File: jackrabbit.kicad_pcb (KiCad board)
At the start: 2 copper layers, 50.3 x 55.4 mm, 56 parts, among them J1 USB_C, J2 PinHeader_2.54mm_02x08, J3 PinHeader_2.54mm_02x08, J4 PinHeader_2.54mm_02x04, J5 PinHeader_2.54mm_02x04, J6 JST_SH_01x04_SM04B-SRSS-TB, J7 PinHeader_2.54mm_01x03, SW1 SW_Push, SW2 SW_Push, U1 MIC5319-3.3YD5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

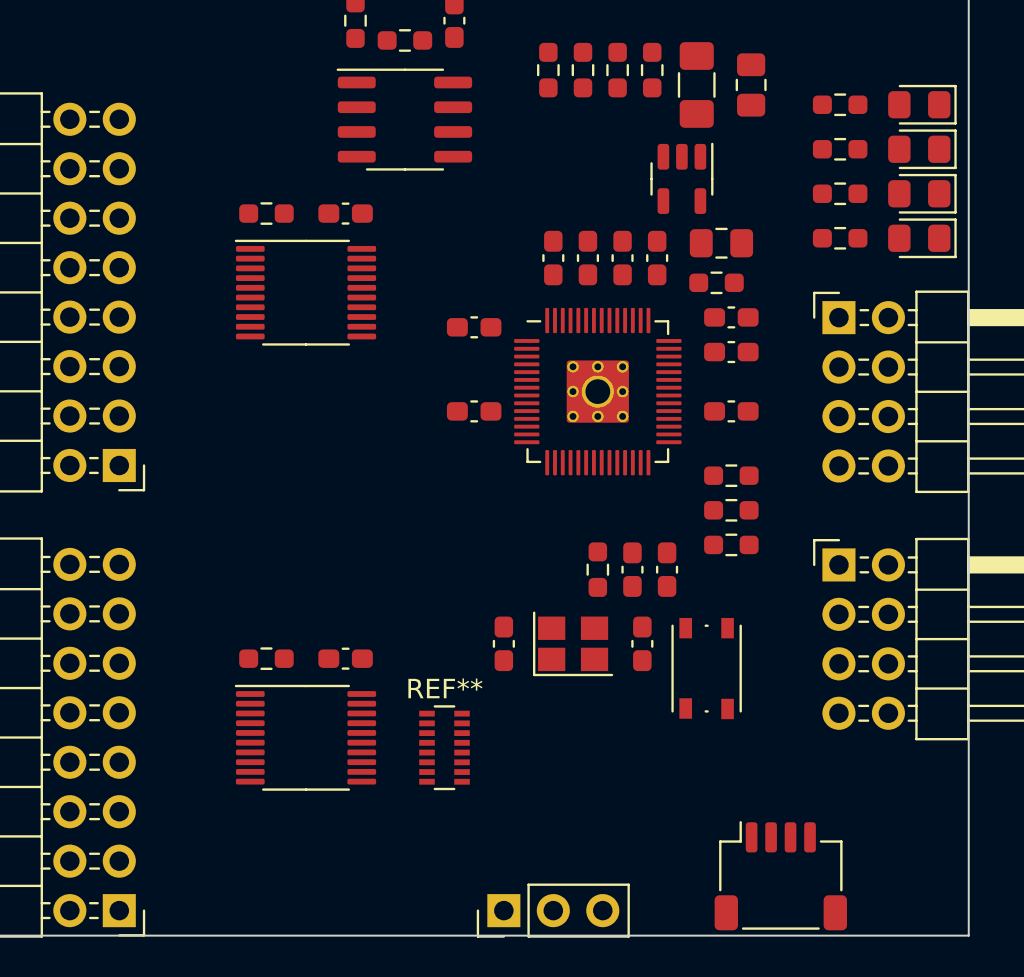
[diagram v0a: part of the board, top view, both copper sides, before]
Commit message: Add bus contention series protection resistors
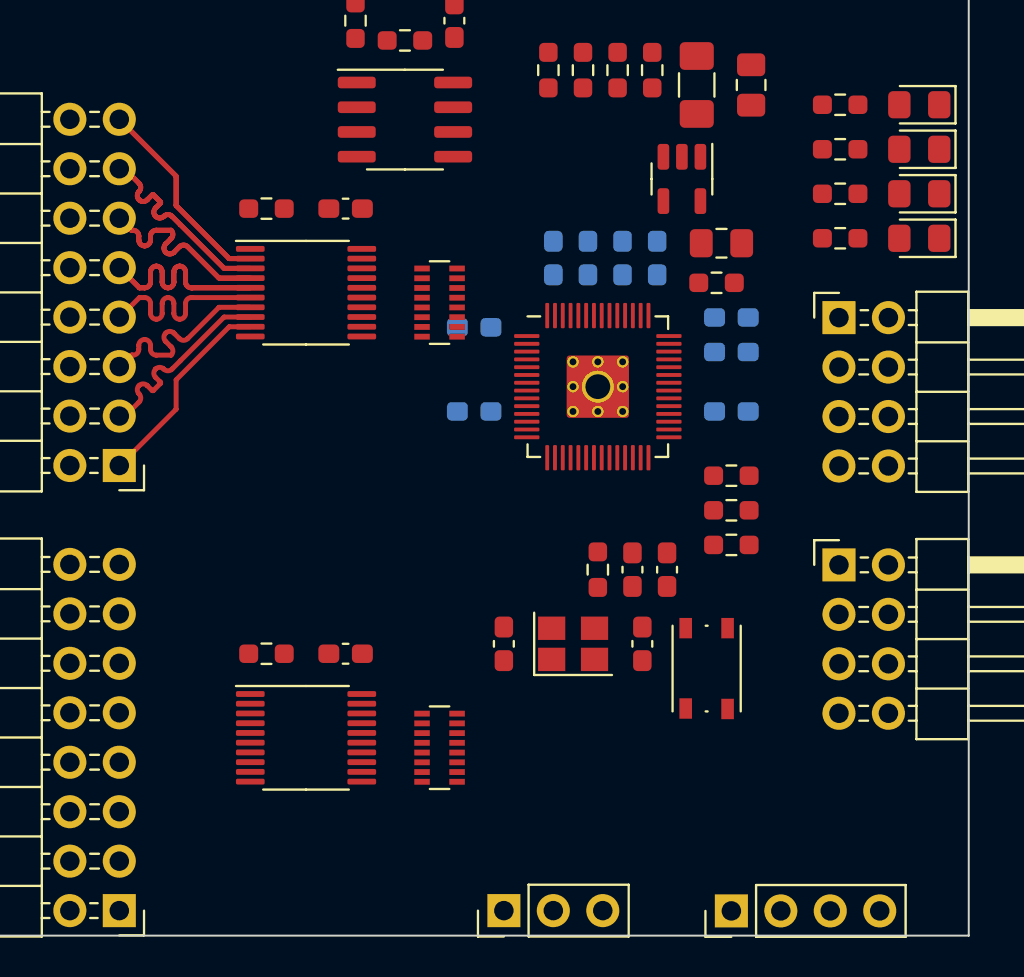
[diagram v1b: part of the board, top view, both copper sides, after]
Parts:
- removed REF**: R_Array_Convex_8x0602, Resistor_SMD:R_Array_Convex_8x0602
- added RN1: 220, Resistor_SMD:R_Array_Convex_8x0602, F.Cu at (144.0, 109.7)
- added RN2: 220, Resistor_SMD:R_Array_Convex_8x0602, F.Cu at (144.0, 132.6)
- C1, C10, C13, C14, C4, C5, C6, C8, C9: moved to B.Cu
- J6: value JST_SH_01x04_SM04B-SRSS-TB -> PinHeader_2.54mm_01x04; footprint Connector_JST:JST_SH_SM04B-SRSS-TB_1x04-1MP_P1.00mm_Horizontal -> Connector_PinHeader_2.54mm:PinHeader_1x04_P2.54mm_Vertical
- R7, R8: value 2.2k -> 100
- moved J6 3.10 mm to (159.0, 141.0), turned to 90 degrees
- moved C11 0.25 mm to (139.2, 104.9)
- moved R9 0.25 mm to (135.1, 104.9)
- moved C16 0.25 mm to (139.2, 127.8)
- moved R12 0.25 mm to (135.1, 127.8)
- moved U4 0.25 mm to (152.1, 114.0)
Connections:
- J6 pad 1: /RX/SDA -> /RX
- J6 pad 2: /TX/SCL -> /TX
- R7 pad 1: /TX/SCL -> Net-(R7-Pad1)
- R7 pad 2: +3V3 -> /TX
- R8 pad 1: /RX/SDA -> Net-(R8-Pad1)
- R8 pad 2: +3V3 -> /RX
- U2 pad 11: /DIG7 -> Net-(RN1-Pad8)
- U2 pad 12: /DIG6 -> Net-(RN1-Pad7)
- U2 pad 13: /DIG5 -> Net-(RN1-Pad6)
- U2 pad 14: /DIG4 -> Net-(RN1-Pad5)
- U2 pad 15: /DIG3 -> Net-(RN1-Pad4)
- U2 pad 16: /DIG2 -> Net-(RN1-Pad3)
- U2 pad 17: /DIG1 -> Net-(RN1-Pad2)
- U2 pad 18: /DIG0 -> Net-(RN1-Pad1)
- U4 pad 29: /TX/SCL -> Net-(R7-Pad1)
- U4 pad 30: /RX/SDA -> Net-(R8-Pad1)
- U5 pad 11: /DIG15 -> Net-(RN2-Pad8)
- U5 pad 12: /DIG14 -> Net-(RN2-Pad7)
- U5 pad 13: /DIG13 -> Net-(RN2-Pad6)
- U5 pad 14: /DIG12 -> Net-(RN2-Pad5)
- U5 pad 15: /DIG11 -> Net-(RN2-Pad4)
- U5 pad 16: /DIG10 -> Net-(RN2-Pad3)
- U5 pad 17: /DIG9 -> Net-(RN2-Pad2)
- U5 pad 18: /DIG8 -> Net-(RN2-Pad1)
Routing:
- net /OUT_DIG0: track 0.00 -> 21.2 mm
- net /OUT_DIG1: track 0.00 -> 21.1 mm
- net /OUT_DIG2: track 0.00 -> 21.0 mm
- net /OUT_DIG3: track 0.00 -> 21.0 mm
- net /OUT_DIG7: track 0.00 -> 10.6 mm
- net /OUT_DIG6: track 0.00 -> 10.6 mm
- net /OUT_DIG5: track 0.00 -> 10.5 mm
- net /OUT_DIG4: track 0.00 -> 10.5 mm

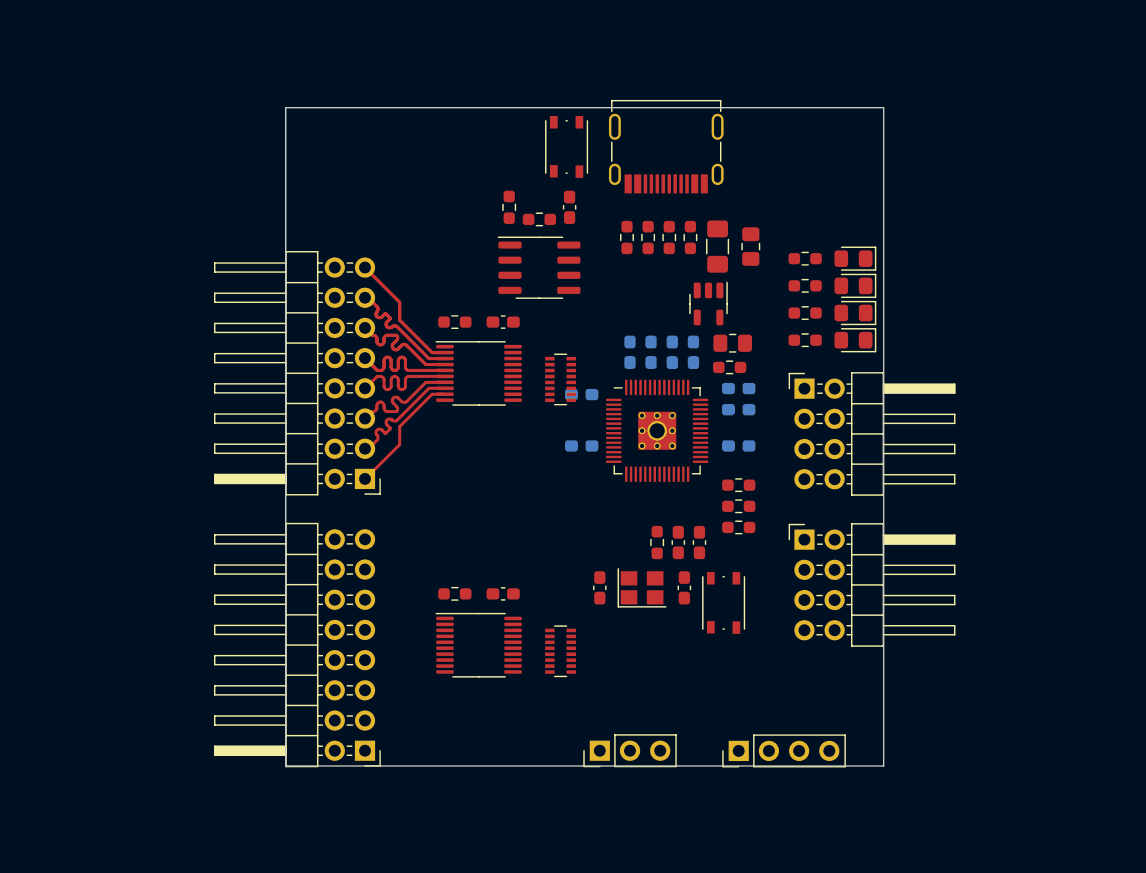
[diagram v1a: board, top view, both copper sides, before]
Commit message: Start layout with passives on bottom
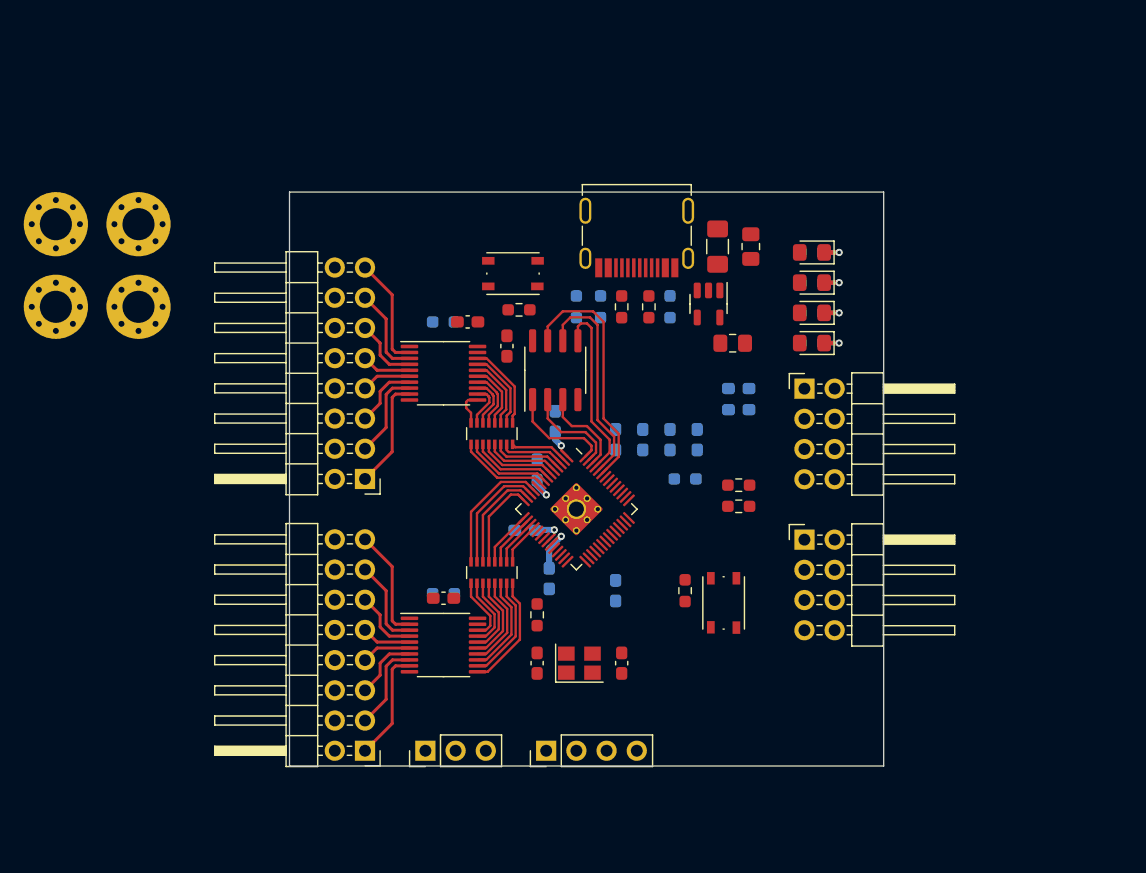
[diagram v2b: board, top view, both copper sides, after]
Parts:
- added H1: M2.5, MountingHole:MountingHole_2.7mm_M2.5_Pad_Via, F.Cu at (108.5, 103.6)
- added H2: M2.5, MountingHole:MountingHole_2.7mm_M2.5_Pad_Via, F.Cu at (101.6, 96.7)
- added H3: M2.5, MountingHole:MountingHole_2.7mm_M2.5_Pad_Via, F.Cu at (108.5, 96.7)
- added H4: M2.5, MountingHole:MountingHole_2.7mm_M2.5_Pad_Via, F.Cu at (101.6, 103.6)
- C12, C7, R1, R10, R12, R14, R15, R16, R17, R2, R3, R9: moved to B.Cu
- moved J6 16.2 mm to (142.8, 141.0)
- moved C6 16.0 mm to (148.7, 127.5), turned to -90 degrees
- moved J7 14.7 mm to (132.7, 141.0)
- moved C12 13.0 mm to (143.1, 126.5)
- moved C7 12.9 mm to (141.0, 122.4), turned to 180 degrees
- moved C15 12.8 mm to (139.5, 106.9), turned to -90 degrees
- moved R11 11.8 mm to (142.0, 129.5)
- moved SW1 11.6 mm to (140.0, 100.8), turned to 0 degrees
- moved R3 10.1 mm to (154.5, 118.1), turned to 180 degrees
- moved R10 10.1 mm to (145.3, 103.6)
- moved U4 9.47 mm to (145.3, 120.6), turned to -45 degrees
- moved RN2 8.79 mm to (138.2, 126.0), turned to 90 degrees
- moved U3 8.72 mm to (143.6, 109.0), turned to 90 degrees
- moved C17 8.24 mm to (142.0, 133.6)
- moved C18 8.24 mm to (149.2, 133.6)
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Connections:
- D1 pad 1: GND -> Net-(D1-Pad1)
- D1 pad 2: Net-(D1-Pad2) -> +5V
- D2 pad 1: GND -> Net-(D2-Pad1)
- D2 pad 2: Net-(D2-Pad2) -> /LEDA
- D3 pad 1: GND -> Net-(D3-Pad1)
- D3 pad 2: Net-(D3-Pad2) -> /LEDB
- D4 pad 1: GND -> Net-(D4-Pad1)
- D4 pad 2: Net-(D4-Pad2) -> /LEDC
- R11 pad 1: Net-(C18-Pad2) -> Net-(C17-Pad2)
- R14 pad 1: +5V -> Net-(D1-Pad1)
- R14 pad 2: Net-(D1-Pad2) -> GND
- R15 pad 1: /LEDA -> Net-(D2-Pad1)
- R15 pad 2: Net-(D2-Pad2) -> GND
- R16 pad 1: /LEDB -> Net-(D3-Pad1)
- R16 pad 2: Net-(D3-Pad2) -> GND
- R17 pad 1: /LEDC -> Net-(D4-Pad1)
- R17 pad 2: Net-(D4-Pad2) -> GND
- U4 pad 20: Net-(C17-Pad2) -> Net-(R11-Pad2)
- U4 pad 21: Net-(R11-Pad2) -> Net-(C18-Pad2)
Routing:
- net /QSPI_SD3: track 0.00 -> 20.6 mm
- net /QSPI_SCLK: track 0.00 -> 18.1 mm
- net /OUT_DIG3: track 21.0 -> 4.16 mm
- net /QSPI_SD0: track 0.00 -> 15.4 mm
- net /OUT_DIG2: track 21.0 -> 5.60 mm
- net /OUT_DIG1: track 21.1 -> 7.49 mm
- net /OUT_DIG0: track 21.2 -> 9.38 mm
- net /DIG8: track 0.00 -> 10.8 mm
- net /DIG9: track 0.00 -> 9.79 mm
- net Net-(RN2-Pad8): track 0.00 -> 9.67 mm
- net /OUT_DIG15: track 0.00 -> 9.38 mm
- net /OUT_DIG8: track 0.00 -> 9.38 mm
- net Net-(RN2-Pad7): track 0.00 -> 9.01 mm
- net /QSPI_SS: track 0.00 -> 8.77 mm
- net /DIG10: track 0.00 -> 8.75 mm
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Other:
- board size 50.3 x 55.4 mm -> 50 x 48.3 mm

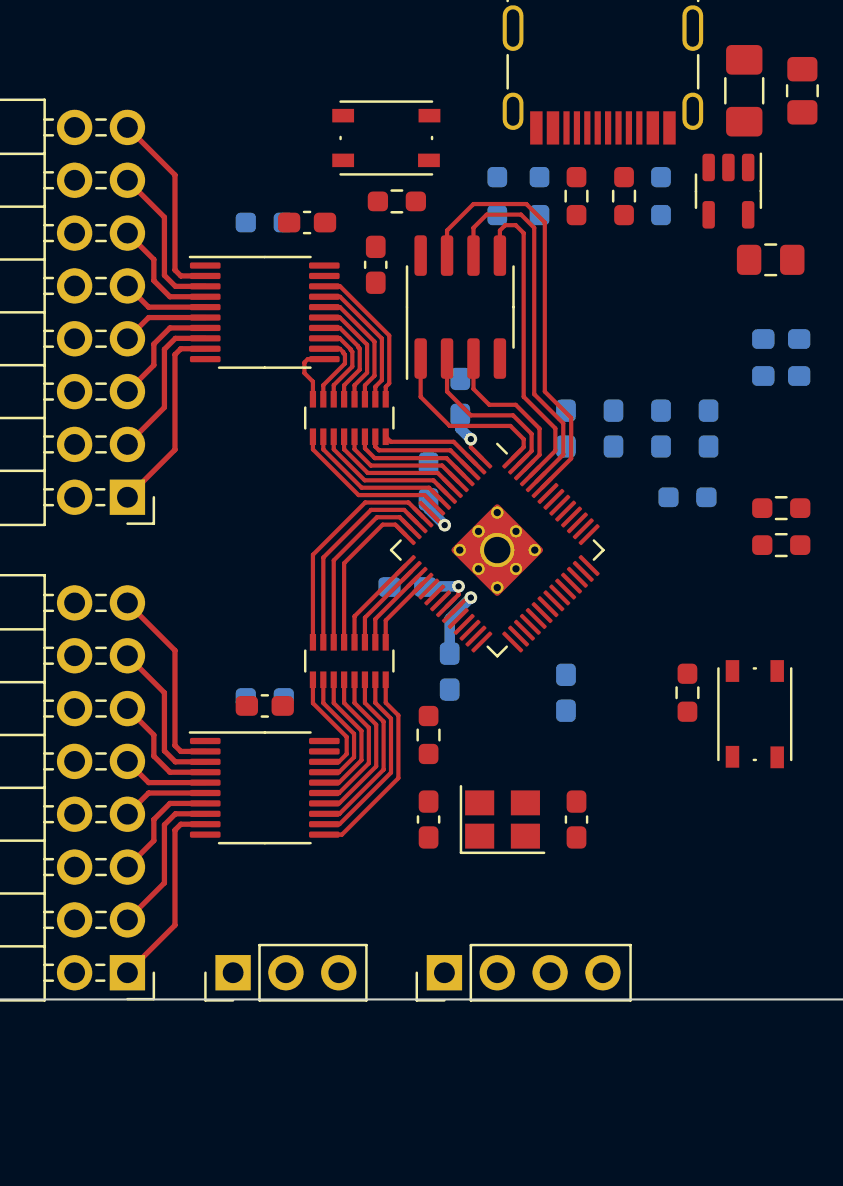
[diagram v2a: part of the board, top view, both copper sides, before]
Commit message: Squeeze buffers together to lower board width
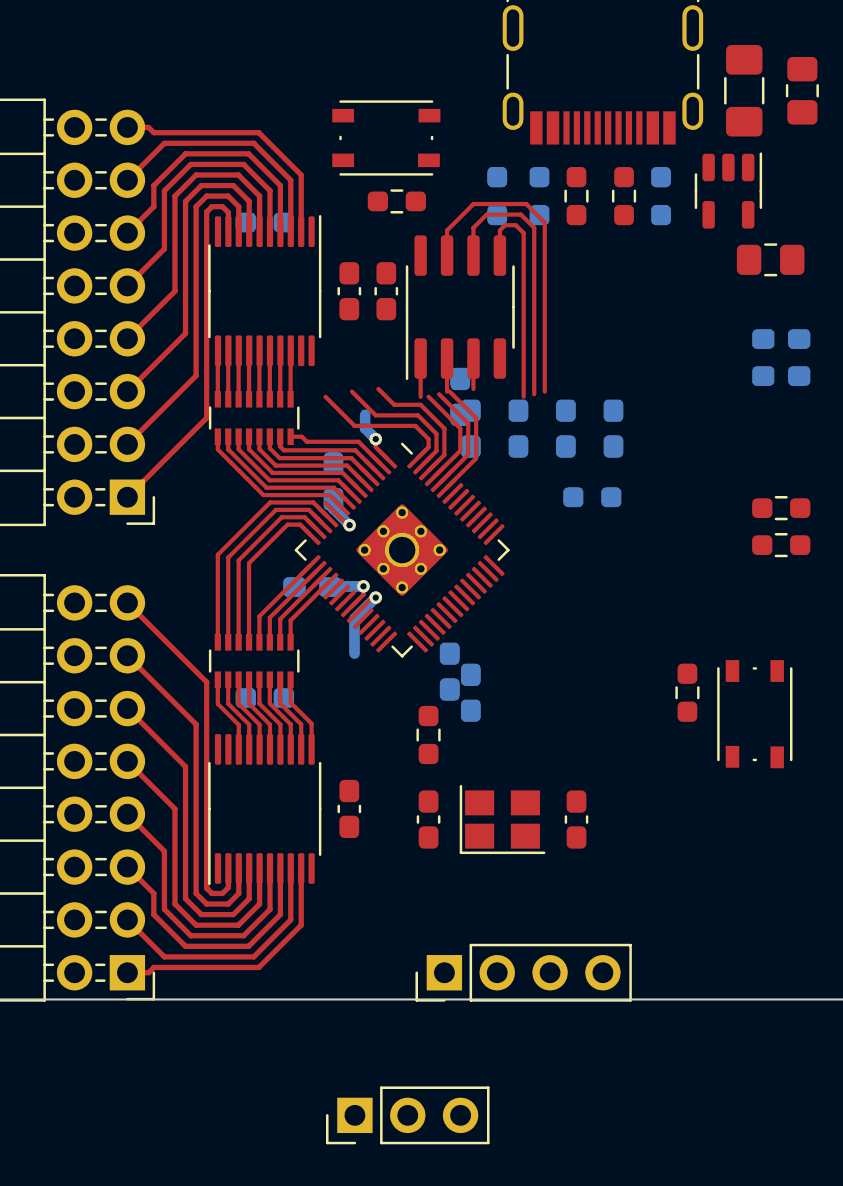
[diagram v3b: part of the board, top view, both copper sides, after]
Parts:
- moved J7 9.02 mm to (138.5, 147.8)
- moved C16 6.41 mm to (138.2, 133.1), turned to -90 degrees
- moved C1 4.57 mm to (150.9, 114.8)
- moved C10 4.57 mm to (148.7, 114.8)
- moved C7 4.57 mm to (136.5, 122.4)
- moved C8 4.57 mm to (137.5, 117.3)
- moved R3 4.57 mm to (149.9, 118.1)
- moved RN1 4.57 mm to (133.7, 114.3)
- moved RN2 4.57 mm to (133.7, 126.0)
- moved U4 4.57 mm to (140.8, 120.6)
- moved C13 4.57 mm to (144.1, 114.8)
- moved C4 4.57 mm to (146.4, 114.8)
- moved C6 4.57 mm to (144.1, 127.5)
- moved C11 3.88 mm to (138.2, 108.2), turned to 90 degrees
- moved C15 1.37 mm to (140.0, 108.2)
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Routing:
- net /OUT_DIG11: track 4.16 -> 14.4 mm
- net /OUT_DIG4: track 4.16 -> 14.4 mm
- net /OUT_DIG5: track 5.60 -> 15.4 mm
- net /OUT_DIG10: track 5.60 -> 15.4 mm
- net /OUT_DIG3: track 4.16 -> 13.4 mm
- net /OUT_DIG12: track 4.16 -> 13.4 mm
- net /OUT_DIG9: track 7.49 -> 16.5 mm
- net /OUT_DIG6: track 7.49 -> 16.5 mm
- net /OUT_DIG8: track 9.38 -> 17.5 mm
- net /OUT_DIG7: track 9.38 -> 17.5 mm
- net /OUT_DIG2: track 5.60 -> 12.4 mm
- net /OUT_DIG13: track 5.60 -> 12.4 mm
- net Net-(RN2-Pad8): track 9.67 -> 3.77 mm
- net Net-(RN2-Pad7): track 9.01 -> 3.77 mm
- net Net-(RN1-Pad1): track 7.24 -> 2.34 mm
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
